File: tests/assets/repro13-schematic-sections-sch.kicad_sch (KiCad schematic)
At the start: 7 parts

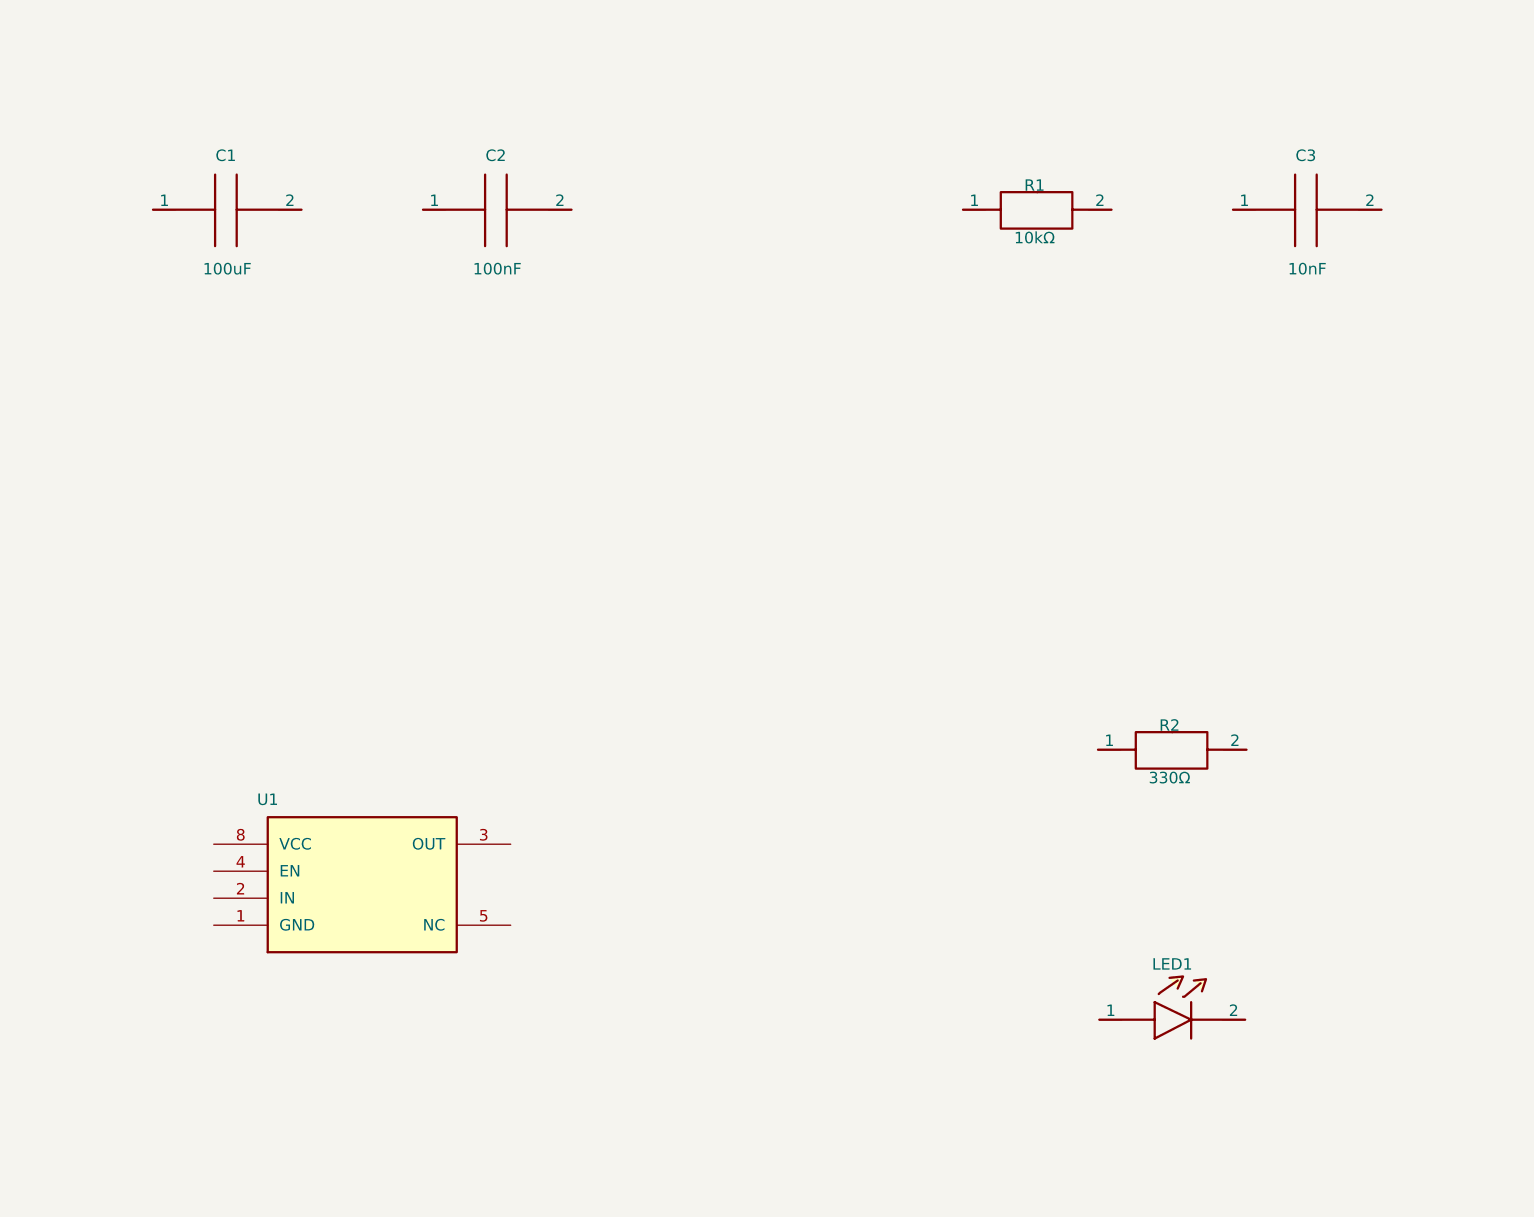
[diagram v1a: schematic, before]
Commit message: Render schematic sections conversion
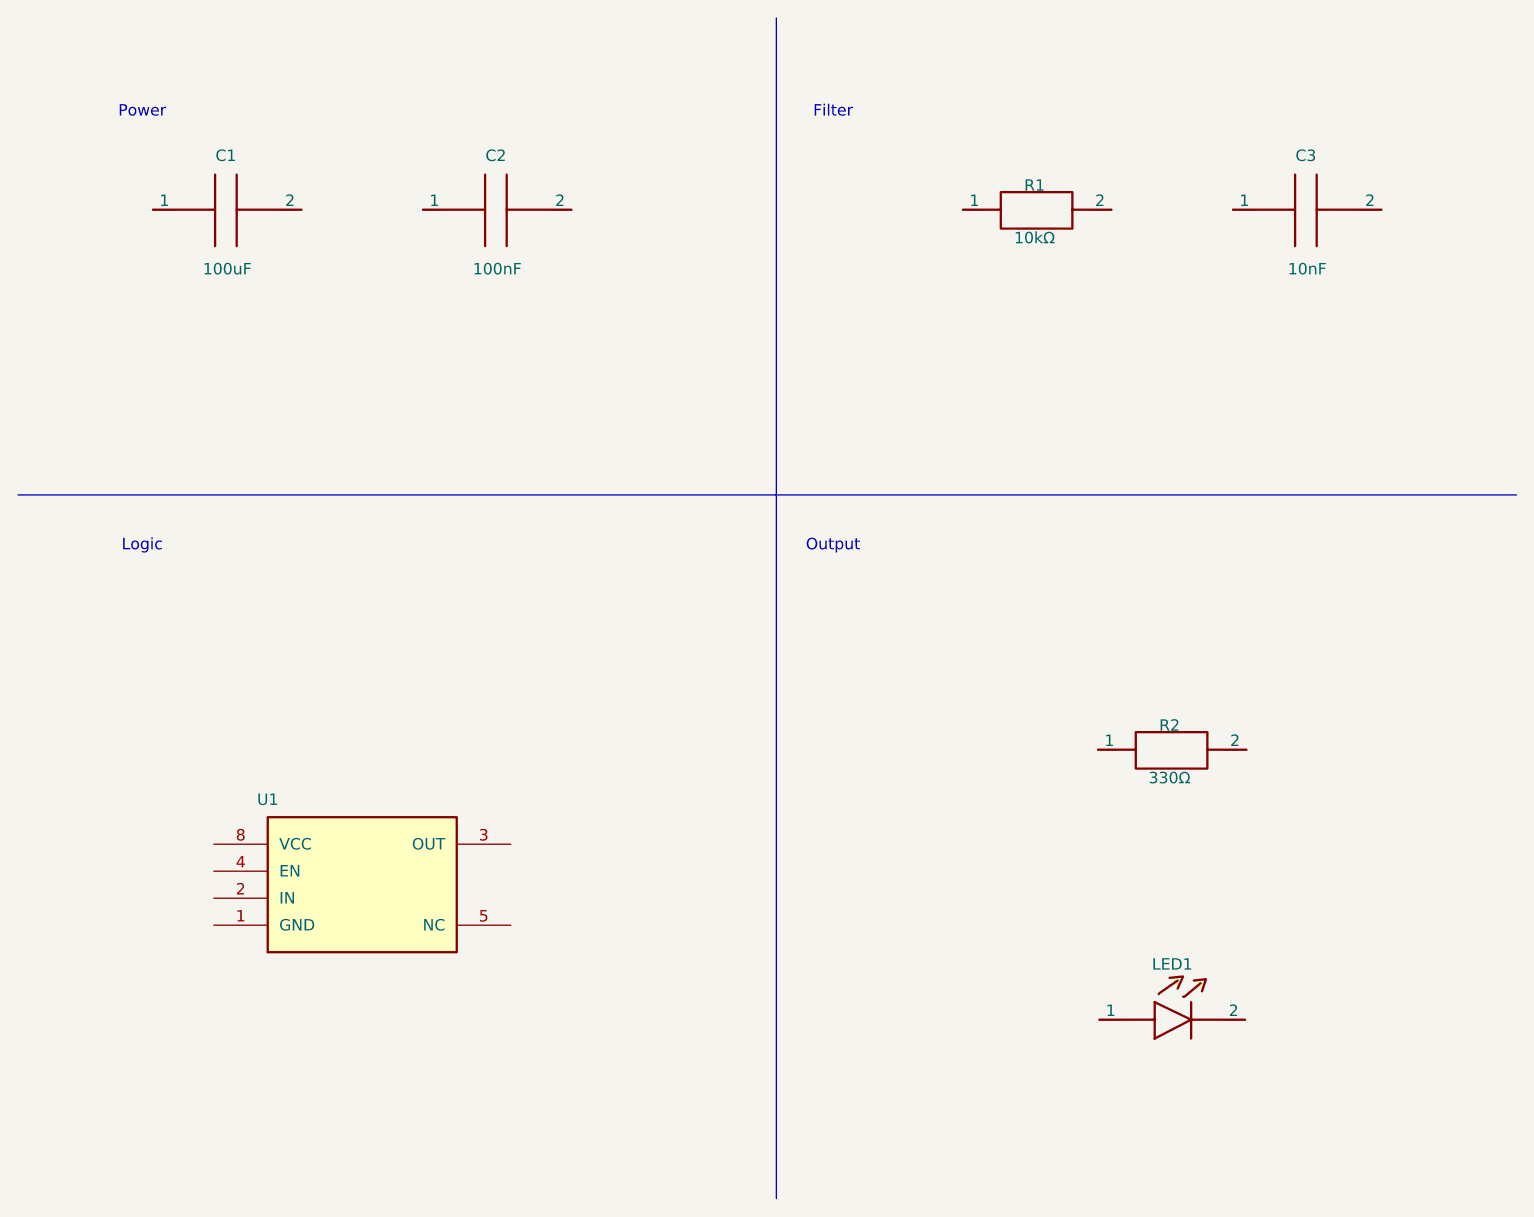
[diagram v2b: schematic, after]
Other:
- note added: "Filter"
- note added: "Logic"
- note added: "Output"
- note added: "Power"
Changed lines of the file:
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@@
     (instances
       (project ""
-        (path "/384f0f5b-5222-4538-8a53-443e61b77923"
+        (path "/932d4e86-f964-48c4-b213-f1aa7ee41f6f"
           (reference "C1")
           (unit 1)
@@
     (instances
       (project ""
-        (path "/384f0f5b-5222-4538-8a53-443e61b77923"
+        (path "/932d4e86-f964-48c4-b213-f1aa7ee41f6f"
           (reference "C2")
           (unit 1)
@@
     (instances
       (project ""
-        (path "/384f0f5b-5222-4538-8a53-443e61b77923"
+        (path "/932d4e86-f964-48c4-b213-f1aa7ee41f6f"
           (reference "R1")
           (unit 1)
@@
     (instances
       (project ""
-        (path "/384f0f5b-5222-4538-8a53-443e61b77923"
+        (path "/932d4e86-f964-48c4-b213-f1aa7ee41f6f"
           (reference "C3")
           (unit 1)
@@
     (instances
       (project ""
-        (path "/384f0f5b-5222-4538-8a53-443e61b77923"
+        (path "/932d4e86-f964-48c4-b213-f1aa7ee41f6f"
           (reference "U1")
           (unit 1)
@@
     (instances
       (project ""
-        (path "/384f0f5b-5222-4538-8a53-443e61b77923"
+        (path "/932d4e86-f964-48c4-b213-f1aa7ee41f6f"
           (reference "R2")
           (unit 1)
@@
     (instances
       (project ""
-        (path "/384f0f5b-5222-4538-8a53-443e61b77923"
+        (path "/932d4e86-f964-48c4-b213-f1aa7ee41f6f"
           (reference "LED1")
           (unit 1)
@@
     )
   )
+  (text "Power"
+    (at 79.05 49.912499999999994 0)
+    (effects
+      (font
+        (size 1.27 1.27)
+        (color 0 0 0 1)
+      )
+    )
+  )
+  (text "Filter"
+    (at 155.8125 49.912499999999994 0)
+    (effects
+      (font
+        (size 1.27 1.27)
+        (color 0 0 0 1)
+      )
+    )
+  )
+  (text "Logic"
+    (at 79.05 98.104084875 0)
+    (effects
+      (font
+        (size 1.27 1.27)
+        (color 0 0 0 1)
+      )
+    )
+  )
+  (text "Output"
+    (at 155.8125 98.104084875 0)
+    (effects
+      (font
+        (size 1.27 1.27)
+        (color 0 0 0 1)
+      )
+    )
+  )
+  (polyline
+    (pts
+      (xy 65.25 92.404084875)
+      (xy 231.75 92.404084875)
+    )
+    (stroke
+      (width 0)
+      (type default)
+      (color 0 0 0 1)
+    )
+  )
+  (polyline
+    (pts
+      (xy 149.5125 170.58749999999998)
+      (xy 149.5125 39.41249999999998)
+    )
+    (stroke
+      (width 0)
+      (type default)
+      (color 0 0 0 1)
+    )
+  )

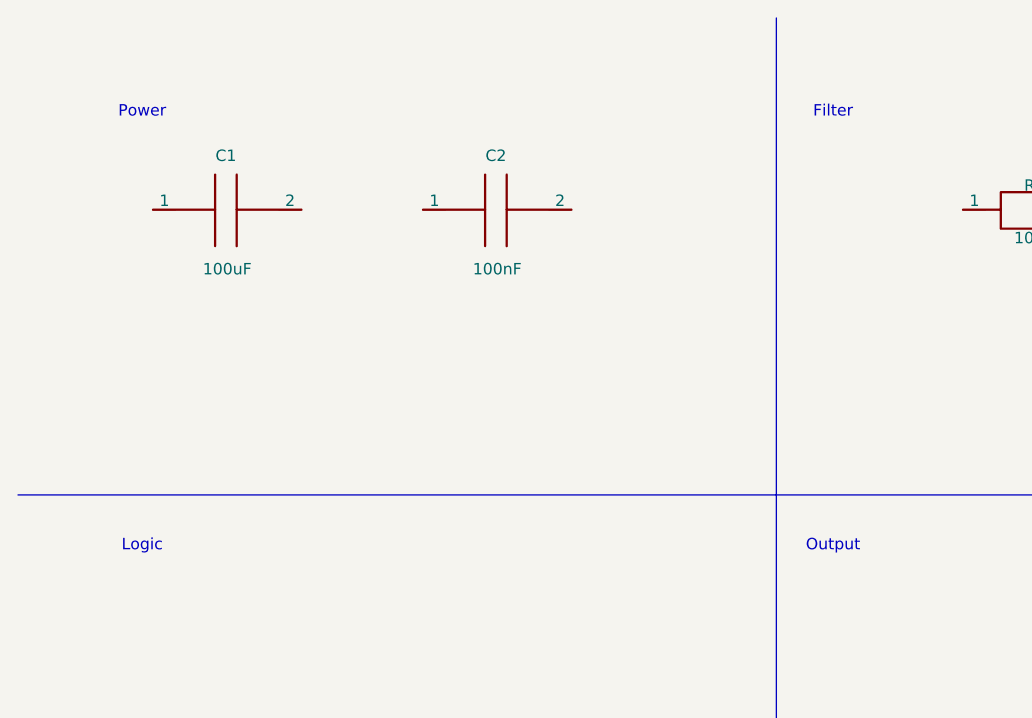
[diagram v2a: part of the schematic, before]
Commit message: Remove schematic section label offsets
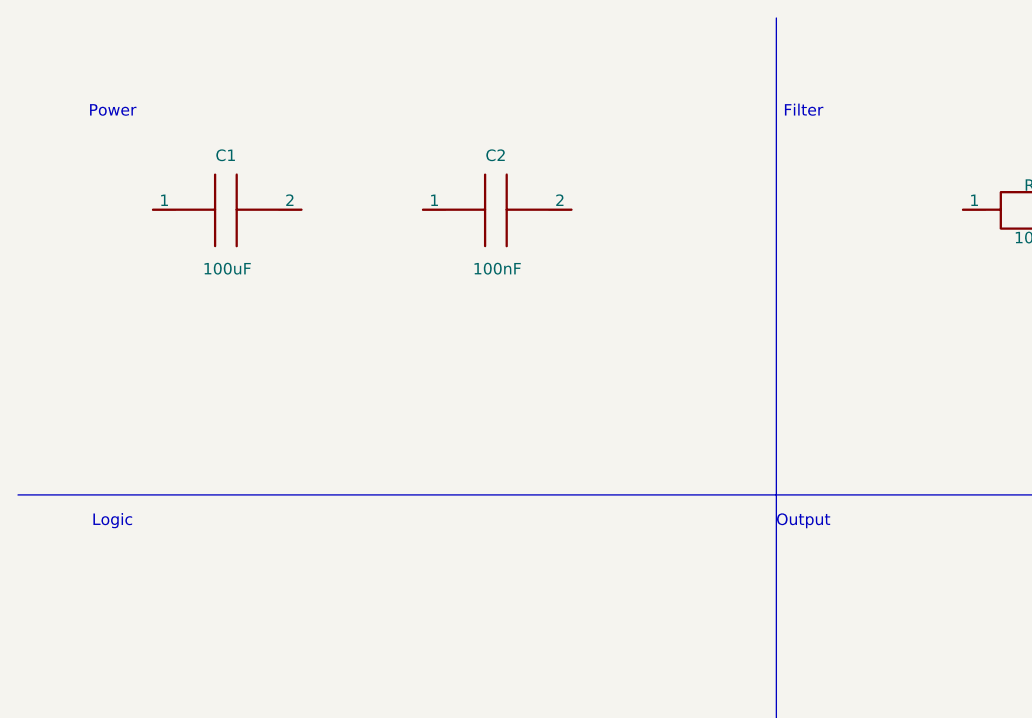
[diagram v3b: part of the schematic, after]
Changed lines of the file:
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@@
     (instances
       (project ""
-        (path "/932d4e86-f964-48c4-b213-f1aa7ee41f6f"
+        (path "/d9d7f3ec-e859-42a6-b49e-5ff8c5576b25"
           (reference "C1")
           (unit 1)
@@
     (instances
       (project ""
-        (path "/932d4e86-f964-48c4-b213-f1aa7ee41f6f"
+        (path "/d9d7f3ec-e859-42a6-b49e-5ff8c5576b25"
           (reference "C2")
           (unit 1)
@@
     (instances
       (project ""
-        (path "/932d4e86-f964-48c4-b213-f1aa7ee41f6f"
+        (path "/d9d7f3ec-e859-42a6-b49e-5ff8c5576b25"
           (reference "R1")
           (unit 1)
@@
     (instances
       (project ""
-        (path "/932d4e86-f964-48c4-b213-f1aa7ee41f6f"
+        (path "/d9d7f3ec-e859-42a6-b49e-5ff8c5576b25"
           (reference "C3")
           (unit 1)
@@
     (instances
       (project ""
-        (path "/932d4e86-f964-48c4-b213-f1aa7ee41f6f"
+        (path "/d9d7f3ec-e859-42a6-b49e-5ff8c5576b25"
           (reference "U1")
           (unit 1)
@@
     (instances
       (project ""
-        (path "/932d4e86-f964-48c4-b213-f1aa7ee41f6f"
+        (path "/d9d7f3ec-e859-42a6-b49e-5ff8c5576b25"
           (reference "R2")
           (unit 1)
@@
     (instances
       (project ""
-        (path "/932d4e86-f964-48c4-b213-f1aa7ee41f6f"
+        (path "/d9d7f3ec-e859-42a6-b49e-5ff8c5576b25"
           (reference "LED1")
           (unit 1)
@@
   )
   (text "Power"
-    (at 79.05 49.912499999999994 0)
+    (at 75.75 49.912499999999994 0)
     (effects
       (font
@@
   )
   (text "Filter"
-    (at 155.8125 49.912499999999994 0)
+    (at 152.5125 49.912499999999994 0)
     (effects
       (font
@@
   )
   (text "Logic"
-    (at 79.05 98.104084875 0)
+    (at 75.75 95.404084875 0)
     (effects
       (font
@@
   )
   (text "Output"
-    (at 155.8125 98.104084875 0)
+    (at 152.5125 95.404084875 0)
     (effects
       (font

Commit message: Refresh schematic sections snapshot
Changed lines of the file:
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@@
     (instances
       (project ""
-        (path "/d9d7f3ec-e859-42a6-b49e-5ff8c5576b25"
+        (path "/be83095d-0909-4ad2-a7fa-ecf97d2a40e9"
           (reference "C1")
           (unit 1)
@@
     (instances
       (project ""
-        (path "/d9d7f3ec-e859-42a6-b49e-5ff8c5576b25"
+        (path "/be83095d-0909-4ad2-a7fa-ecf97d2a40e9"
           (reference "C2")
           (unit 1)
@@
     (instances
       (project ""
-        (path "/d9d7f3ec-e859-42a6-b49e-5ff8c5576b25"
+        (path "/be83095d-0909-4ad2-a7fa-ecf97d2a40e9"
           (reference "R1")
           (unit 1)
@@
     (instances
       (project ""
-        (path "/d9d7f3ec-e859-42a6-b49e-5ff8c5576b25"
+        (path "/be83095d-0909-4ad2-a7fa-ecf97d2a40e9"
           (reference "C3")
           (unit 1)
@@
     (instances
       (project ""
-        (path "/d9d7f3ec-e859-42a6-b49e-5ff8c5576b25"
+        (path "/be83095d-0909-4ad2-a7fa-ecf97d2a40e9"
           (reference "U1")
           (unit 1)
@@
     (instances
       (project ""
-        (path "/d9d7f3ec-e859-42a6-b49e-5ff8c5576b25"
+        (path "/be83095d-0909-4ad2-a7fa-ecf97d2a40e9"
           (reference "R2")
           (unit 1)
@@
     (instances
       (project ""
-        (path "/d9d7f3ec-e859-42a6-b49e-5ff8c5576b25"
+        (path "/be83095d-0909-4ad2-a7fa-ecf97d2a40e9"
           (reference "LED1")
           (unit 1)
@@
   )
   (text "Power"
-    (at 75.75 49.912499999999994 0)
+    (at 79.05 49.912499999999994 0)
     (effects
       (font
@@
   )
   (text "Filter"
-    (at 152.5125 49.912499999999994 0)
+    (at 155.8125 49.912499999999994 0)
     (effects
       (font
@@
   )
   (text "Logic"
-    (at 75.75 95.404084875 0)
+    (at 79.05 98.104084875 0)
     (effects
       (font
@@
   )
   (text "Output"
-    (at 152.5125 95.404084875 0)
+    (at 155.8125 98.104084875 0)
     (effects
       (font
